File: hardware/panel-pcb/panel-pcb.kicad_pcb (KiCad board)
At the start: 4 copper layers, 135 x 131 mm, 129 parts, among them J1 USB_C_Receptacle_USB2.0_16P, J10 RS-485 OUT, J11 12V_OUT, J2 SWD, J3 FSR North, J4 FSR East, J5 12V_IN, J6 FSR South, J7 FSR West, J8 RS-485 IN, J9 INT OUT, SW1 PANEL_ID, SW2 BOOTSEL, SW3 RS-485 Termination, U1 RP2040, U2 THVD1419, U3 W25Q32JV, U4 SN74AHCT125, U5 AMS1117-5.0, U6 AMS1117-3.3, X1 12MHz

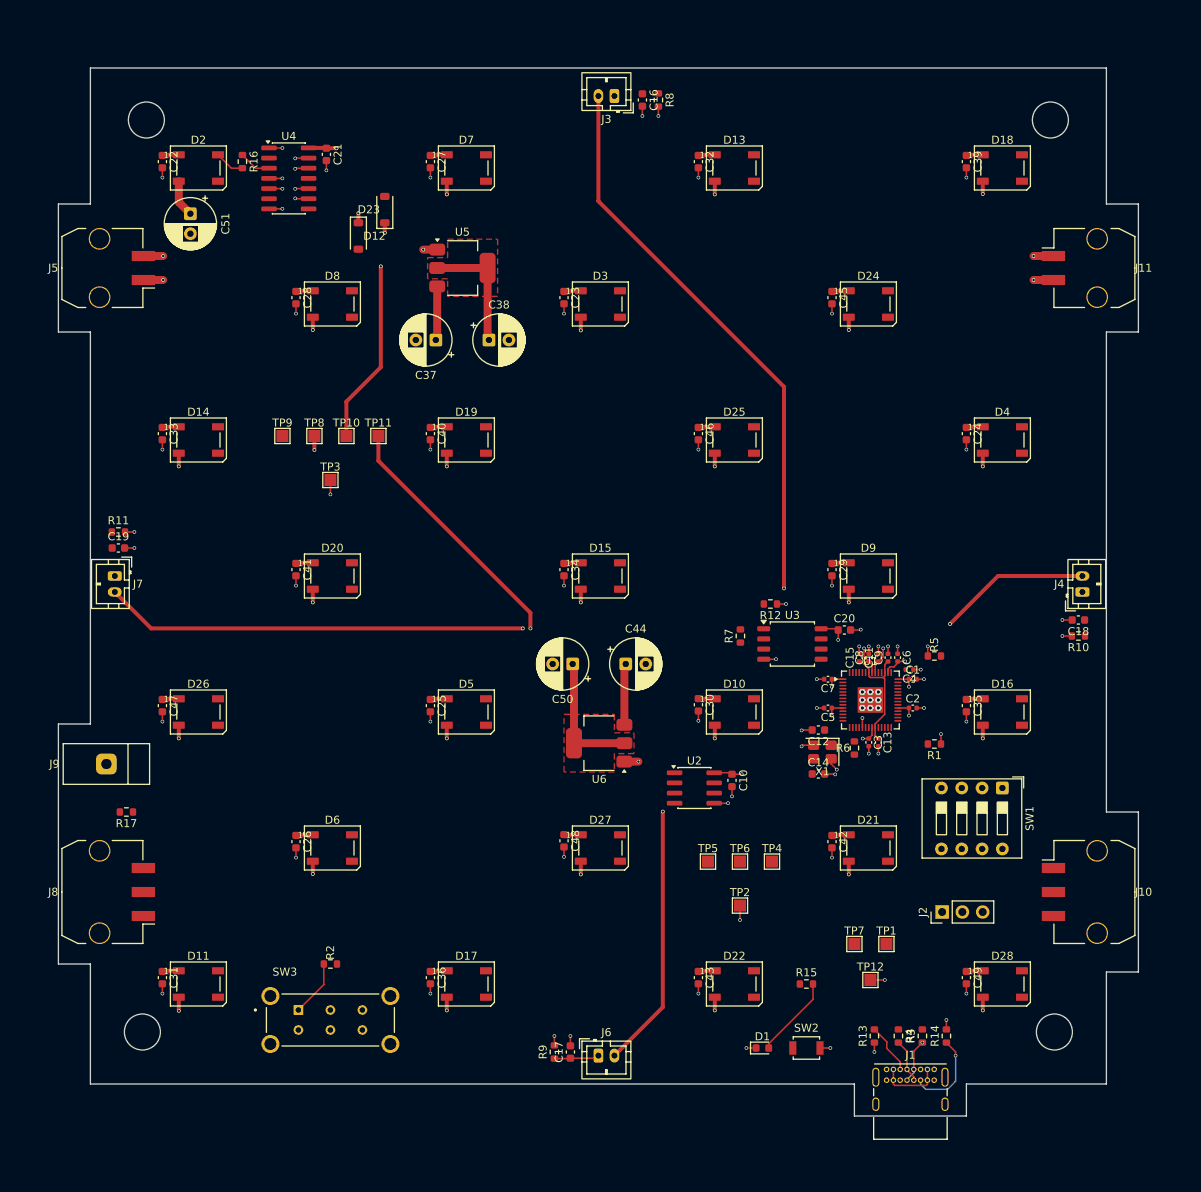
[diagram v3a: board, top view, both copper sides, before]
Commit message: Panel PCB: 12V transition via fixes, JLC DRC rule tuning, schematic field parity
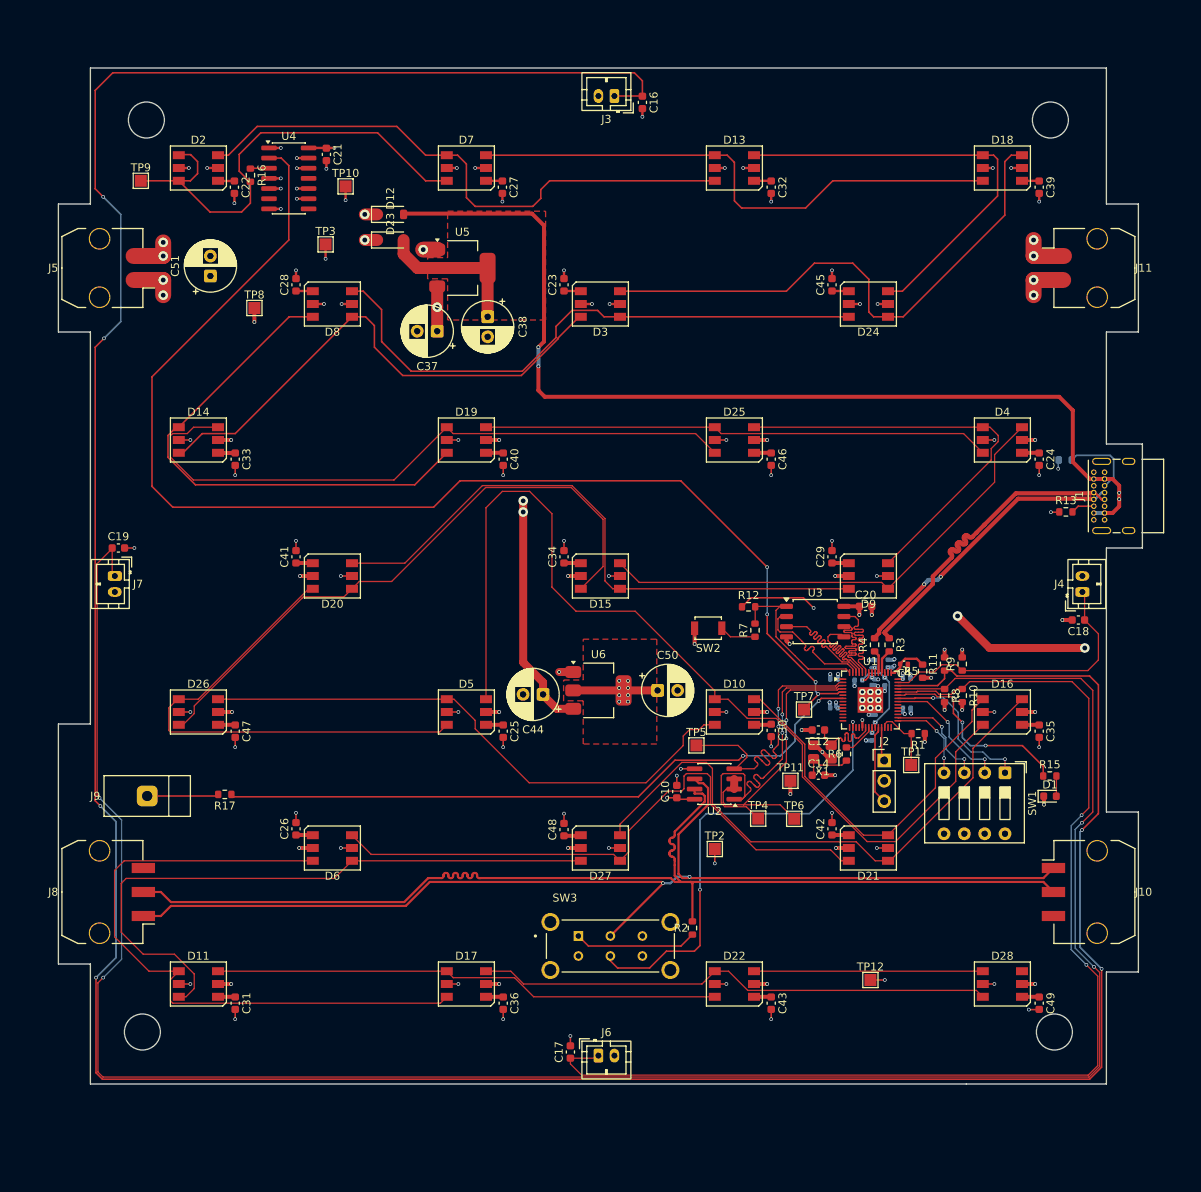
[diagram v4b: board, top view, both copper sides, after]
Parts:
- C1, C11, C13, C15, C2, C3, C5, C6, C7, C8, C9, R14: moved to B.Cu
- D10, D11, D13, D14, D15, D16, D17, D18, D19, D2, D20, D21, D22, D24, D25, D26, D27, D28, D3, D4, D5, D6, D7, D8, D9: footprint LED_SMD:LED_WS2812B_PLCC4_5.0x5.0mm_P3.2mm -> panel-pcb:WS2815_PLCC6_5.0x5.0mm_P1.6mm
- moved R11 104.6 mm to (156.8, 124.5), turned to 90 degrees
- moved R8 82.6 mm to (156.8, 128.4)
- moved R14 73.5 mm to (171.8, 99.0), turned to 180 degrees
- moved J1 73.4 mm to (175.4, 106.5), turned to 90 degrees
- moved R9 70.4 mm to (159.0, 124.5)
- moved R13 69.7 mm to (171.9, 105.5), turned to 0 degrees
- moved TP11 67.2 mm to (137.5, 139.1)
- moved SW2 53.9 mm to (127.2, 120.0), turned to 180 degrees
- moved R3 49.1 mm to (149.8, 122.1), turned to -90 degrees
- moved R4 49.0 mm to (148.0, 122.1), turned to 90 degrees
- moved D1 47.8 mm to (169.9, 141.0)
- moved R2 45.5 mm to (125.2, 157.5), turned to 90 degrees
- moved R15 40.0 mm to (169.9, 138.5)
- moved TP9 36.5 mm to (56.3, 64.1)
- moved SW3 36.2 mm to (115.0, 159.8)
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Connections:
- net Net-(U1-USB_DM) renamed /USB-
- net Net-(U1-USB_DP) renamed /USB+
- net RS485_A renamed RS485+
- net RS485_B renamed RS485-
- net USB_DM renamed USB_D-
- net USB_DP renamed USB_D+
- C16 pad 1: GPIO26/ADC0 -> GPIO28/ADC2
- C17 pad 1: GPIO28/ADC2 -> GPIO26/ADC0
- C18 pad 1: GPIO27/ADC1 -> GPIO29/ADC3
- C19 pad 1: GPIO29/ADC3 -> GPIO27/ADC1
- D2 pad 4: Net-(D2-BIN) -> /LD0
- J3 pad 1: GPIO26/ADC0 -> GPIO28/ADC2
- J4 pad 1: GPIO27/ADC1 -> GPIO29/ADC3
- J6 pad 1: GPIO28/ADC2 -> GPIO26/ADC0
- J7 pad 1: GPIO29/ADC3 -> GPIO27/ADC1
- R10 pad 1: GPIO27/ADC1 -> GPIO26/ADC0
- R11 pad 1: GPIO29/ADC3 -> GPIO28/ADC2
- R15 pad 1: GPIO3 -> GPIO25
- R16 pad 2: Net-(D2-BIN) -> /LD0
- R8 pad 1: GPIO26/ADC0 -> GPIO27/ADC1
- R9 pad 1: GPIO28/ADC2 -> GPIO29/ADC3
- SW1 pad 1: GPIO6 -> GPIO24
- SW1 pad 2: GPIO7 -> GPIO23
- SW1 pad 3: GPIO8 -> GPIO19
- SW1 pad 4: GPIO9 -> GPIO18
- SW3 pad 5: GPIO10 -> GPIO13
- TP7 pad 1: GPIO16 -> GPIO3
- TP9 pad 1: Net-(D2-BIN) -> /LD0
- U4 pad 2: GPIO16 -> GPIO3
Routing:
- net GPIO28/ADC2: track 5.66 -> 406.4 mm, vias 0 -> 6
- net GPIO27/ADC1: track 0.00 -> 273.2 mm, vias 0 -> 4
- net +3V3: track 256.4 -> 58.6 mm, vias 18 -> 30
- net GPIO3: track 0.00 -> 158.2 mm, vias 0 -> 4
- net GPIO26/ADC0: track 0.00 -> 145.1 mm, vias 0 -> 2
- net RS485+: track 0.00 -> 141.9 mm, vias 0 -> 2
- net RS485-: track 0.00 -> 140.5 mm
- net /LD16: track 0.00 -> 121.6 mm
- net VBUS: track 8.08 -> 126.4 mm, vias 1 -> 4
- net GPIO5: track 0.00 -> 82.9 mm, vias 0 -> 2
- net /LD21: track 0.00 -> 82.5 mm
- net /LD8: track 0.00 -> 82.4 mm
- net /LD20: track 0.00 -> 80.2 mm
- net /LD13: track 0.00 -> 77.4 mm
- net /LD19: track 0.00 -> 77.0 mm
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- added copper zone on In2.Cu, net VBUS
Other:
- board size 135 x 131 mm -> 135.5 x 127 mm

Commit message: Panel PCB: AP7361C 3V3 LDO + PMEG3015EH swap, THT Micro-Fit connectors, docs reconciliation
Hardware (schematic + PCB + user re-routing):
- U6 AMS1117-3.3 -> AP7361C-33ER-13 (-33ER- suffix only; low dropout fixes
  USB-VBUS-only powering headroom), D12/D23 1N5819W -> PMEG3015EH
- Caps re-specced all-SMD: C38 22uF 16V tantalum (ESR for AMS1117-5.0 out),
  C37+new C52 parallel 10uF 0805 MLCC (12V DC-bias fix), C44/C50 10uF MLCC,
  C51 470uF -> SMD V-chip electrolytic RVT1E471M1010
- J5/J8/J10/J11 Micro-Fit swapped SMD (43650-0210/-0310) -> right-angle THT
  (43650-0200/-0300); the old BOM "43651" series pointer was wrong

Docs: full staleness pass cross-referenced against schematic/PCB/memory —
STATUS.md rewritten to current state; stale AMS1117-3.3/1N5819W/INT-2-pin/
USB-C-TBD/34mm-pitch/no-remote references fixed across CLAUDE.md, BOM,
schematic plan, layout notes (+ routing width conventions folded in from
scratch notes), RS-485 protocol, underglow, measurements docs.
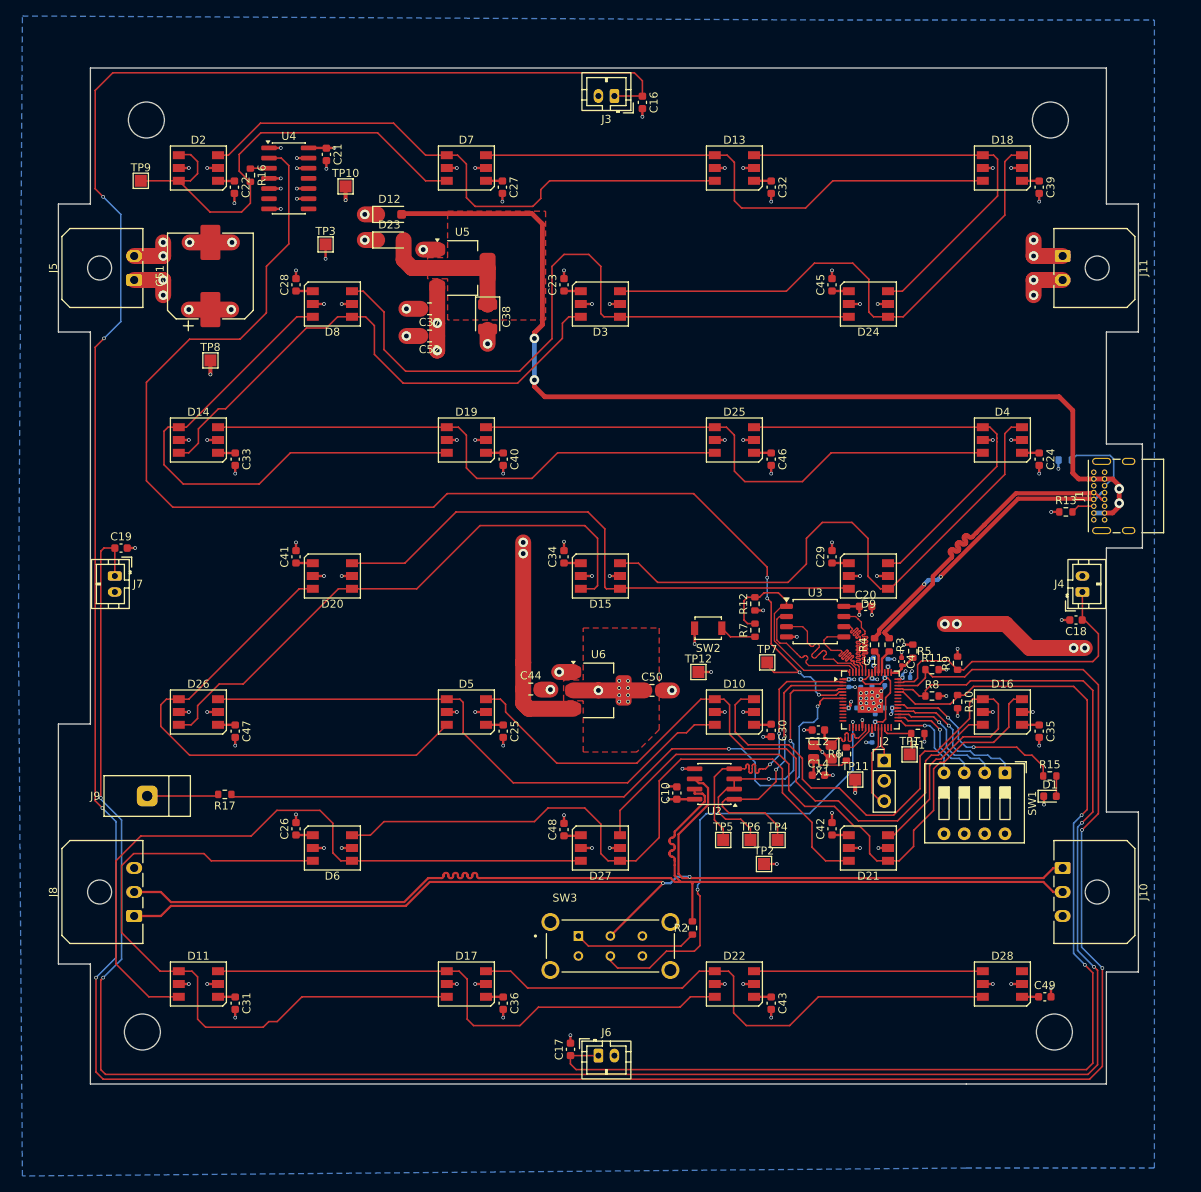
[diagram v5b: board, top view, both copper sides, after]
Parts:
- added C52: 10uF X5R 25V, Capacitor_SMD:C_0805_2012Metric, F.Cu at (92.4, 83.5)
- C37, C44: value 10uF elec 25V -> 10uF X5R 25V; footprint Capacitor_THT:CP_Radial_D6.3mm_P2.50mm -> Capacitor_SMD:C_0805_2012Metric
- C38: value 22uF elec 25V -> 22uF tant 16V; footprint Capacitor_THT:CP_Radial_D6.3mm_P2.50mm -> Capacitor_Tantalum_SMD:CP_EIA-3528-21_Kemet-B
- C50: value 22uF elec 25V -> 10uF X5R 25V; footprint Capacitor_THT:CP_Radial_D6.3mm_P2.50mm -> Capacitor_SMD:C_0805_2012Metric
- C51: footprint Capacitor_THT:CP_Radial_D6.3mm_P2.50mm -> Capacitor_SMD:CP_Elec_10x10.5
- D12, D23: value 1N5819W -> PMEG3015EH; footprint Diode_SMD:D_SOD-123 -> Diode_SMD:D_SOD-123F
- J10, J8: footprint Connector_Molex:Molex_Micro-Fit_3.0_43650-0310_1x03-1MP_P3.00mm_Horizontal -> Connector_Molex:Molex_Micro-Fit_3.0_43650-0300_1x03_P3.00mm_Horizontal
- J11, J5: footprint Connector_Molex:Molex_Micro-Fit_3.0_43650-0210_1x02-1MP_P3.00mm_Horizontal -> Connector_Molex:Molex_Micro-Fit_3.0_43650-0200_1x02_P3.00mm_Horizontal
- U6: value AMS1117-3.3 -> AP7361C-33ER-13
- moved TP12 44.1 mm to (126.0, 125.5)
- moved TP5 12.3 mm to (129.1, 146.5)
- moved TP8 8.55 mm to (65.0, 86.5)
- moved TP11 8.10 mm to (145.6, 138.9)
- moved TP7 7.48 mm to (134.6, 124.3)
- moved TP2 6.43 mm to (134.2, 149.5)
- moved TP6 6.08 mm to (132.5, 146.5)
- moved J10 4.98 mm to (171.5, 150.0)
- moved J8 4.98 mm to (55.5, 156.0)
- moved J11 4.24 mm to (171.5, 73.5)
- moved J5 4.24 mm to (55.5, 76.5)
- moved TP4 3.61 mm to (135.9, 146.5)
- moved C37 2.96 mm to (92.4, 80.1)
- moved R5 2.78 mm to (152.8, 122.9), turned to -90 degrees
- moved C5 2.32 mm to (145.3, 130.0), turned to 0 degrees
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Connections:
- R15 pad 1: GPIO25 -> GPIO22
- SW1 pad 1: GPIO24 -> GPIO21
- SW1 pad 2: GPIO23 -> GPIO20
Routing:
- net /LD16: track 121.6 -> 86.8 mm
- net /LD17: track 48.1 -> 79.5 mm
- net GPIO25: track 25.4 -> 0.00 mm, vias 3 -> 0
- net GPIO22: track 0.00 -> 23.4 mm, vias 0 -> 2
- net GPIO24: track 20.2 -> 0.00 mm, vias 2 -> 0
- net GPIO21: track 0.00 -> 18.5 mm, vias 0 -> 1
- net GPIO23: track 16.5 -> 0.00 mm, vias 2 -> 0
- net GPIO20: track 0.00 -> 15.8 mm, vias 0 -> 1
- net /LD5: track 72.9 -> 87.0 mm
- net /LD8: track 82.4 -> 68.5 mm
- net /LD11: track 62.0 -> 73.8 mm
- net /LD19: track 77.0 -> 86.7 mm
- net +3V3: track 58.6 -> 49.0 mm, vias 30 -> 32
- net GPIO5: track 82.9 -> 91.6 mm
- net /LD20: track 80.2 -> 87.9 mm
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- added copper zone on B.Cu, net GND

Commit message: Panel PCB: USBLC6-2SC6 USB ESD array (U7), island GND stitching vias, routing touch-ups
- Add USBLC6-2SC6 (U7) on the USB-C data lines, connector side of the
  27R series resistors, flow-through routed with a local GND via.
  Rationale: shoe-on-rubber tribocharging on the pad, not just bench
  plug events. Docs updated (CLAUDE.md, BOM, schematic plan).
- GND stitching vias for the In2 island regions (zone-priority net
  inheritance issue resolved; no +12V free vias remain).
- Minor trace adjustments from the via pass. DRC clean: 0 violations,
  0 unconnected.
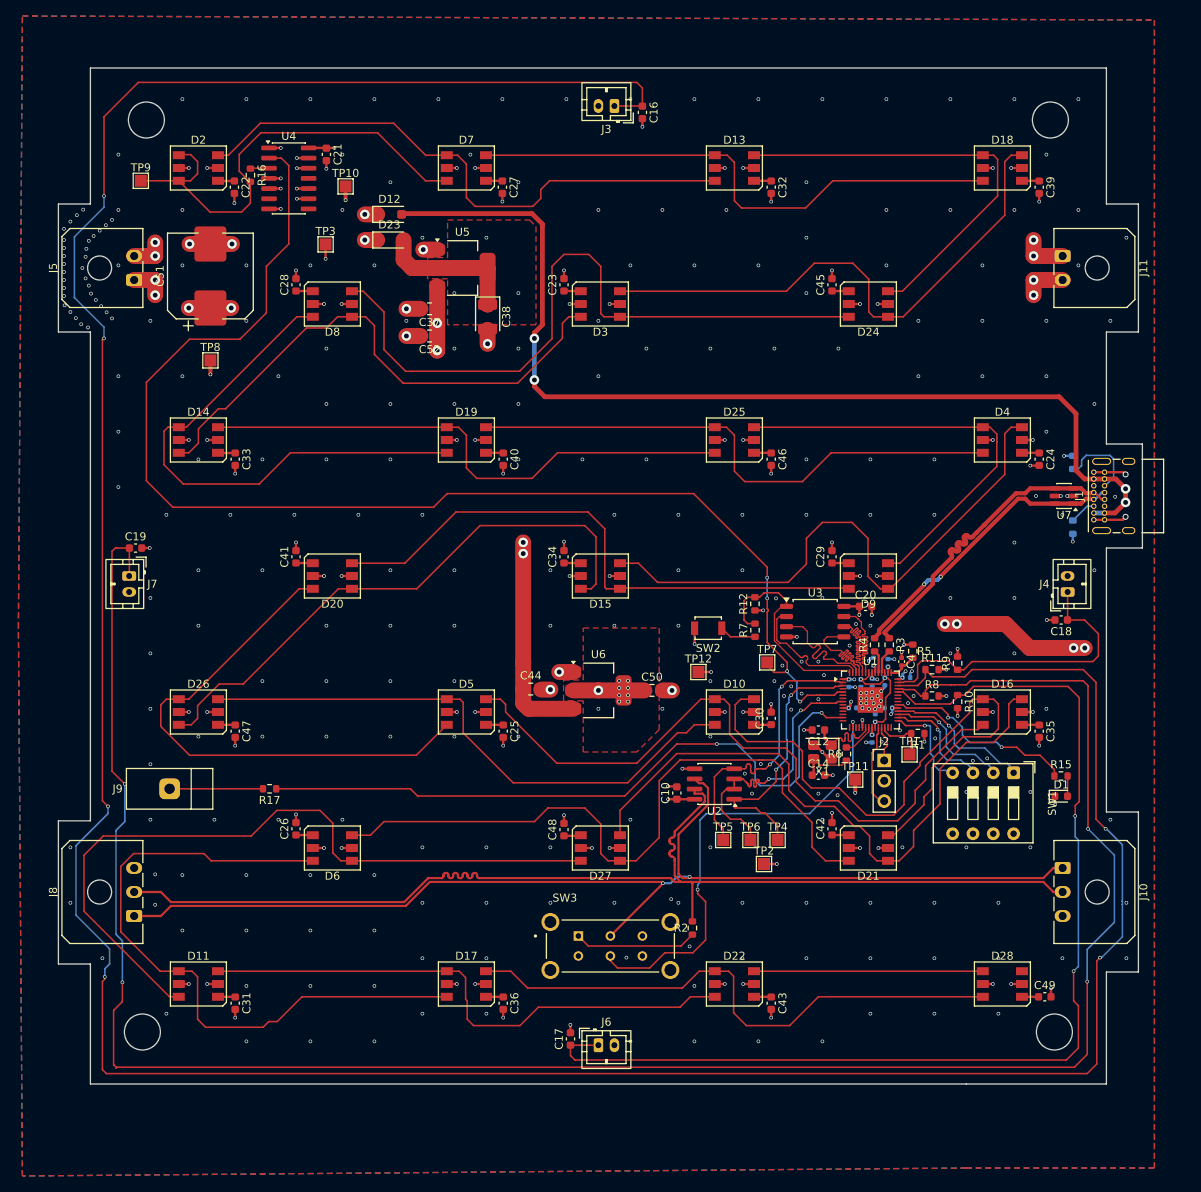
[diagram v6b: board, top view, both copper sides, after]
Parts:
- added U7: USBLC6-2SC6, Package_TO_SOT_SMD:SOT-23-6, F.Cu at (171.7, 103.5)
- R13: moved to B.Cu
- moved R17 5.64 mm to (72.4, 140.1)
- moved J9 2.94 mm to (59.9, 140.1)
- moved R13 2.10 mm to (172.8, 107.4), turned to 90 degrees
- moved C18 1.85 mm to (171.3, 119.0)
- moved J4 1.85 mm to (172.2, 115.5)
- moved C19 1.81 mm to (55.6, 110.0)
- moved J7 1.80 mm to (54.9, 113.5)
- moved C30 1.50 mm to (135.1, 131.3), turned to 90 degrees
- moved D1 1.40 mm to (171.3, 141.0)
- moved R15 1.40 mm to (171.3, 138.5)
- moved C17 1.30 mm to (110.0, 171.4)
- moved J6 1.30 mm to (113.5, 172.2)
- moved C16 1.25 mm to (119.0, 55.5)
- moved J3 1.25 mm to (115.5, 54.8)
- moved SW1 1.08 mm to (165.4, 138.1)
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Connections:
- R17 pad 1: GPIO5 -> GPIO10
- TP6 pad 1: GPIO2 -> GPIO6
- U2 pad 2: GPIO2 -> GPIO6
- U2 pad 3: GPIO2 -> GPIO6
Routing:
- net GPIO5: track 91.6 -> 0.01 mm, vias 2 -> 0
- net GPIO10: track 0.00 -> 85.1 mm, vias 0 -> 2
- net GPIO2: track 36.2 -> 0.00 mm, vias 2 -> 0
- net GPIO6: track 0.00 -> 35.9 mm, vias 0 -> 2
- net GND: track 136.4 -> 144.2 mm, vias 117 -> 391
- net GPIO26/ADC0: track 143.6 -> 138.7 mm
- net /LD20: track 87.9 -> 92.5 mm
- net GPIO27/ADC1: track 272.8 -> 269.0 mm
- net GPIO1: track 37.3 -> 33.9 mm
- net Net-(J9-Pin_1): track 8.96 -> 11.7 mm
- net GPIO28/ADC2: track 407.1 -> 404.6 mm
- net GPIO29/ADC3: track 37.3 -> 39.2 mm
- net GPIO0: track 37.8 -> 36.1 mm
- net VBUS: track 127.4 -> 128.8 mm, vias 4 -> 5
- net GPIO18: track 10.9 -> 12.2 mm
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- added copper zone on F.Cu, net GND
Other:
- outline, holes or cut-outs redrawn
